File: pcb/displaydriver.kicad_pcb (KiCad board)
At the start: 2 copper layers, 65 x 70 mm, 6 parts, among them J1 Screw_Terminal_1x02, U1 Teensy3.1, U2 TXB0108-PW, U3 TXB0108-PW, U4 RGBLEDMTX

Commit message: Rev 1.0 PCB
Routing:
- net +3V3: track 69.6 -> 80.2 mm
- net Net-(U1-Pad5): track 22.8 -> 26.1 mm
- net Net-(U1-Pad9): track 22.8 -> 25.5 mm
- net Net-(U1-Pad7): track 22.8 -> 25.5 mm
- net Net-(U1-Pad11): track 22.8 -> 25.5 mm
- net Net-(U1-Pad24): track 19.1 -> 21.6 mm
- net Net-(U1-Pad8): track 22.8 -> 25.3 mm
- net Net-(U1-Pad6): track 22.8 -> 25.3 mm
- net Net-(U1-Pad4): track 22.8 -> 25.3 mm
- net Net-(U1-Pad25): track 18.9 -> 21.5 mm
- net Net-(U1-Pad22): track 19.5 -> 22.1 mm
- net Net-(U1-Pad21): track 19.3 -> 21.8 mm
- net Net-(U1-Pad10): track 22.8 -> 25.3 mm
- net Net-(U1-Pad23): track 19.0 -> 21.5 mm
- removed copper zone on B.Cu, net GND
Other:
- board text added: "Michael Cullen January 2016"
- board text removed: "Michael Cullen 2016"

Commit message: Final changes for bodgetastic pcb v1.0
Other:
- board text added: "Michael Cullen January 2017"
- board text added: "https://michaelcullen.name"
- board text removed: "Michael Cullen January 2016"
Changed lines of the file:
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@@
     (area 104.949999 71.920951 170.050001 145.050001)
     (thickness 1.6)
-    (drawings 8)
+    (drawings 9)
     (tracks 130)
     (zones 0)
@@
       (net 3 +3V3))
   )
-  (gr_text "Michael Cullen\nJanuary 2016" (at 116.84 139.954) (layer B.Cu)
+  (gr_text https://michaelcullen.name (at 151.384 141.732) (layer B.SilkS)
     (effects (font (size 1.5 1.5) (thickness 0.3)) (justify mirror))
   )
+  (gr_text "Michael Cullen\nJanuary 2017" (at 116.84 139.954) (layer B.Cu)
+    (effects (font (size 1.5 1.5) (thickness 0.3)) (justify mirror))
+  )

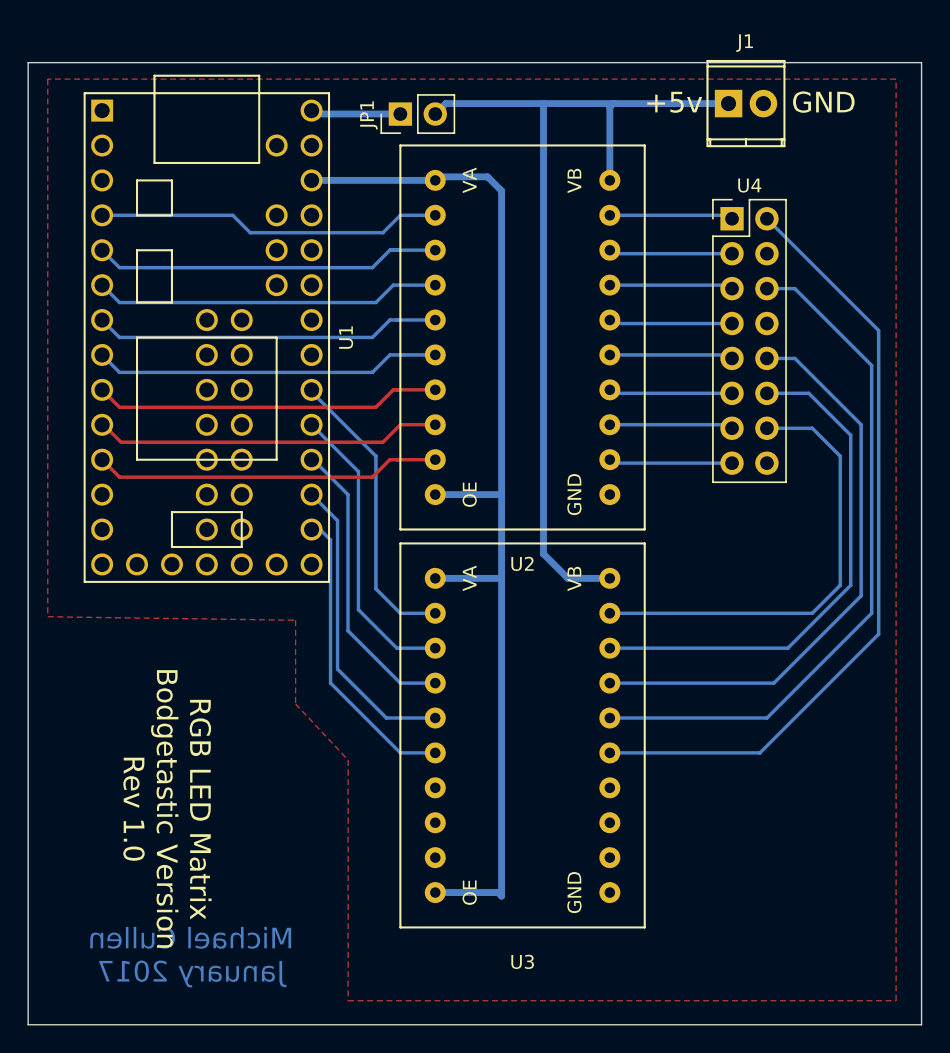
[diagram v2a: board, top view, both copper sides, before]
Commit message: Fixed a few PCB bugs and annoyances found on first run
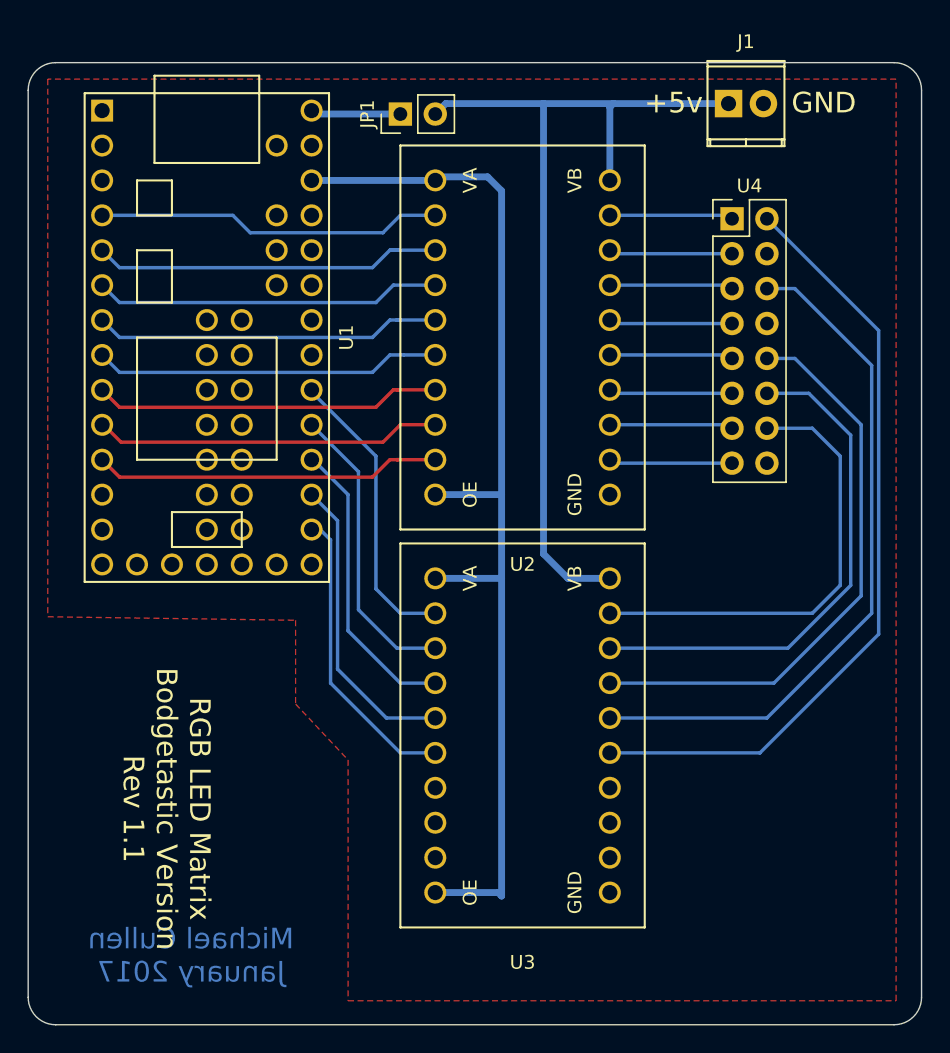
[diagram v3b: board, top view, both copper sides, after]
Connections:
- U4 pad 16: (no net) -> GND
- U4 pad 4: (no net) -> GND
- U4 pad 8: (no net) -> GND
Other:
- outline, holes or cut-outs redrawn
- board text added: "RGB LED Matrix Bodgetastic Version Rev 1.1"
- board text removed: "RGB LED Matrix Bodgetastic Version Rev 1.0"

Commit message: Swapped power plug out for barrel jack, left PCB partially unrouted since future changes are likely
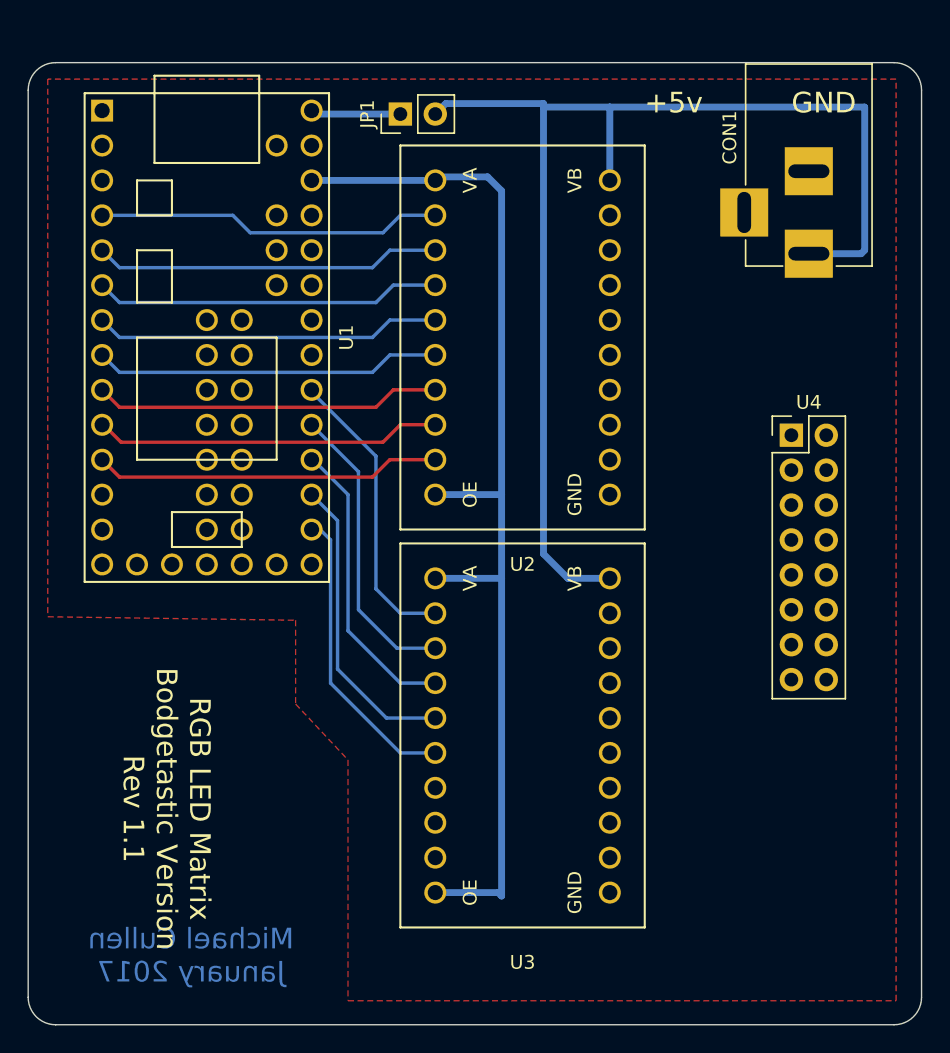
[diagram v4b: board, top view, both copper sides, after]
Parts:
- removed J1: Screw_Terminal_1x02, Connectors_Terminal_Blocks:TerminalBlock_Pheonix_MPT-2.54mm_2pol
- added CON1: BARREL_JACK, Connectors:BARREL_JACK, F.Cu at (161.8, 88.9)
- moved U4 16.3 mm to (160.5, 102.1)
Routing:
- net Net-(U3-Pad15): track 56.7 -> 0.00 mm
- net Net-(U3-Pad16): track 50.2 -> 0.00 mm
- net Net-(U3-Pad17): track 42.2 -> 0.00 mm
- net Net-(U3-Pad18): track 37.7 -> 0.00 mm
- net Net-(U3-Pad20): track 33.2 -> 0.00 mm
- net +5V: track 65.7 -> 89.8 mm
- net Net-(U2-Pad20): track 9.00 -> 0.00 mm
- net Net-(U2-Pad17): track 9.00 -> 0.00 mm
- net Net-(U2-Pad15): track 9.00 -> 0.00 mm
- net Net-(U2-Pad13): track 9.00 -> 0.00 mm
- net Net-(U2-Pad18): track 9.00 -> 0.36 mm
- net Net-(U2-Pad16): track 9.00 -> 0.36 mm
- net Net-(U2-Pad14): track 9.00 -> 0.36 mm
- net Net-(U2-Pad12): track 9.00 -> 0.36 mm
- net Net-(U1-Pad5): track 26.1 -> 25.3 mm

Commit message: PCB 1.1
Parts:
- added J1: Screw_Terminal_1x02, Connectors_Terminal_Blocks:TerminalBlock_Pheonix_PT-3.5mm_2pol, F.Cu at (164.6, 99.1)
- moved U4 7.37 mm to (160.5, 109.5)
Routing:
- net Net-(U3-Pad15): track 0.00 -> 55.6 mm
- net Net-(U3-Pad16): track 0.00 -> 48.7 mm
- net Net-(U3-Pad17): track 0.00 -> 39.8 mm
- net Net-(U3-Pad18): track 0.00 -> 37.0 mm
- net Net-(U2-Pad20): track 0.00 -> 32.7 mm
- net Net-(U2-Pad17): track 0.00 -> 32.6 mm
- net Net-(U2-Pad18): track 0.36 -> 32.6 mm
- net Net-(U2-Pad16): track 0.36 -> 32.5 mm
- net Net-(U2-Pad15): track 0.00 -> 32.0 mm
- net Net-(U2-Pad14): track 0.36 -> 31.9 mm
- net Net-(U3-Pad20): track 0.00 -> 31.4 mm
- net Net-(U2-Pad13): track 0.00 -> 31.1 mm
- net Net-(U2-Pad12): track 0.36 -> 31.1 mm
- net GND: track 0.36 -> 27.9 mm
- net +5V: track 89.8 -> 97.6 mm
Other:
- net class High Power added: clearance 0.2, trace_width 2, via_dia 0.6, via_drill 0.4
- board text added: "Michael Cullen June 2017"
- board text removed: "Michael Cullen January 2017"

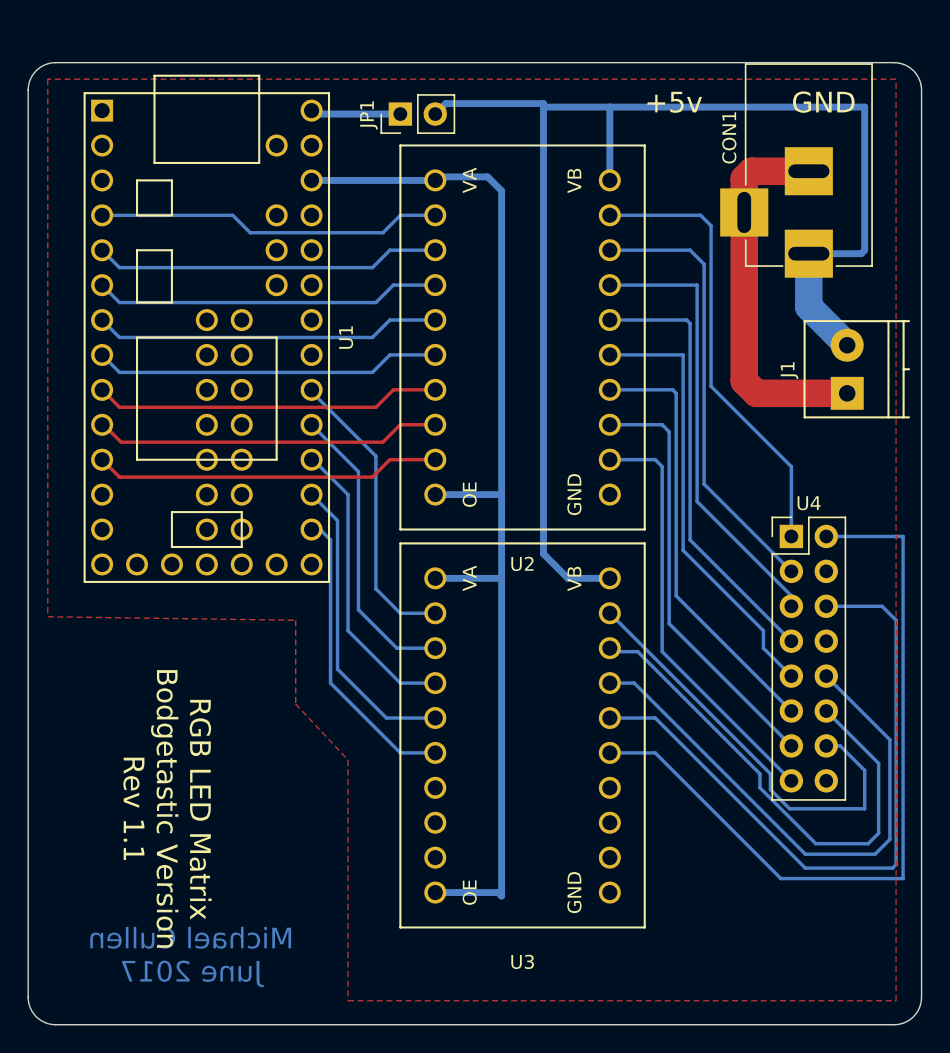
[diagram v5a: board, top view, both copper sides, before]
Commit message: PCB: Fixed some silkscreen issues
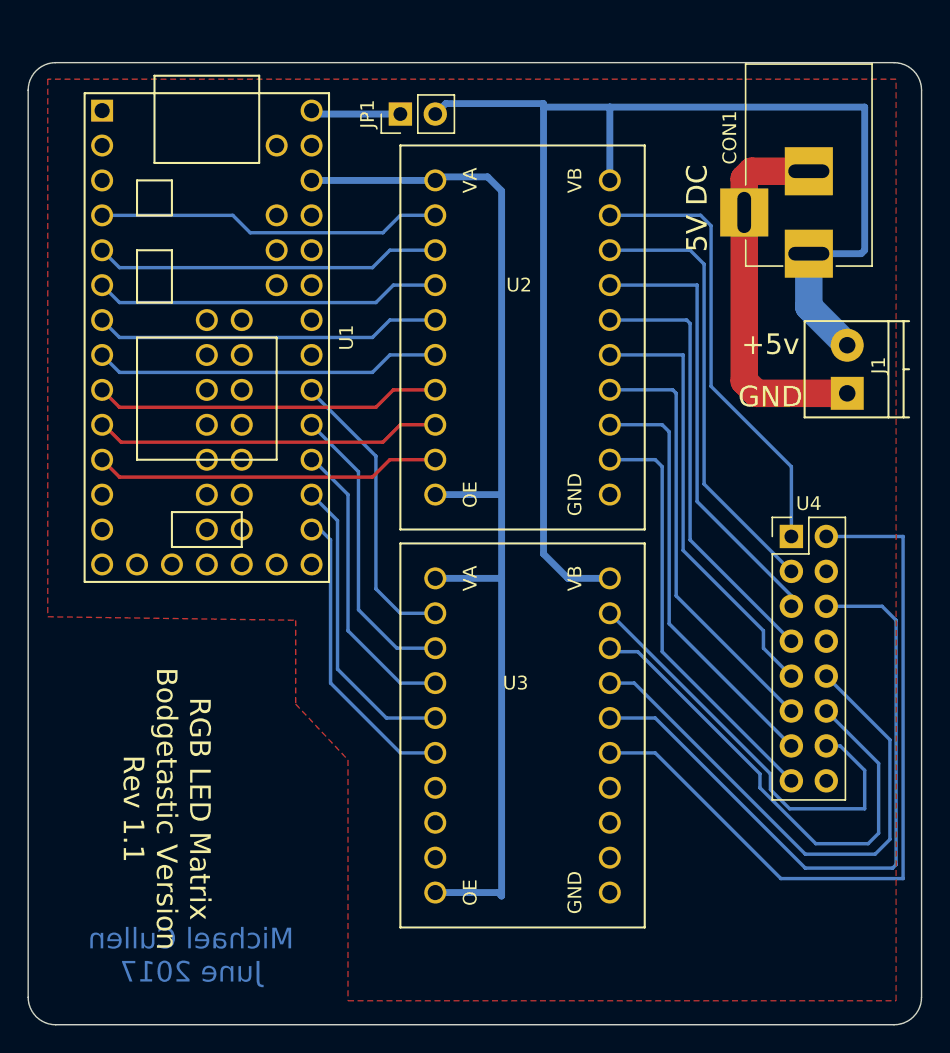
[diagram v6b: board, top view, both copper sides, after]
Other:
- board text added: "5V DC"
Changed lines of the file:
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@@
     (area 104.949999 74.949999 170.050001 145.050001)
     (thickness 1.6)
-    (drawings 13)
+    (drawings 14)
     (tracks 163)
     (zones 0)
@@
   (module txb0108_breakout:txb0108_breakout (layer F.Cu)
     (at 137.16 120.142 270)
-    (fp_text reference U3 (at 20.32 -3.81 360) (layer F.SilkS)
+    (fp_text reference U3 (at 0 -3.302 360) (layer F.SilkS)
       (effects (font (size 1 1) (thickness 0.15)))
     )
@@
   (module txb0108_breakout:txb0108_breakout (layer F.Cu)
     (at 137.16 91.186 270)
-    (fp_text reference U2 (at 20.32 -3.81 360) (layer F.SilkS)
+    (fp_text reference U2 (at 0 -3.556 360) (layer F.SilkS)
       (effects (font (size 1 1) (thickness 0.15)))
     )
@@
     (at 164.592 99.06 90)
     (descr "2-way 3.5mm pitch terminal block, Phoenix PT series")
-    (fp_text reference J1 (at 1.75 -4.3 90) (layer F.SilkS)
+    (fp_text reference J1 (at 2.032 2.286 90) (layer F.SilkS)
       (effects (font (size 1 1) (thickness 0.15)))
     )
@@
     )
   )
+  (gr_text "5V DC" (at 153.67 85.598 90) (layer F.SilkS)
+    (effects (font (size 1.5 1.5) (thickness 0.3)))
+  )
+  (gr_text +5v (at 159.004 95.504) (layer F.SilkS)
+    (effects (font (size 1.5 1.5) (thickness 0.3)))
+  )
+  (gr_text GND (at 159.004 99.314) (layer F.SilkS)
+    (effects (font (size 1.5 1.5) (thickness 0.3)))
+  )
   (gr_arc (start 107 77) (end 105 77) (angle 90) (layer Edge.Cuts) (width 0.1))
   (gr_arc (start 107 143) (end 107 145) (angle 90) (layer Edge.Cuts) (width 0.1))
@@
   (gr_line (start 170 77) (end 170 143) (angle 90) (layer Edge.Cuts) (width 0.1))
   (gr_line (start 107 75) (end 168 75) (angle 90) (layer Edge.Cuts) (width 0.1))
-  (gr_text GND (at 162.8902 77.9272) (layer F.SilkS)
-    (effects (font (size 1.5 1.5) (thickness 0.3)))
-  )
-  (gr_text +5v (at 151.9682 77.9272) (layer F.SilkS)
-    (effects (font (size 1.5 1.5) (thickness 0.3)))
-  )
   (segment (start 164.592 99.06) (end 157.988 99.06) (width 2) (layer F.Cu) (net 1))
   (segment (start 157.098 98.17) (end 157.098 85.9) (width 2) (layer F.Cu) (net 1))
